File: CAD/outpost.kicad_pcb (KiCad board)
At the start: 2 copper layers, 10 parts, among them U1 SHT41-AD1F-R2, U1 SHT4x, U2 AS7343xDLG, U3 NBM5100B

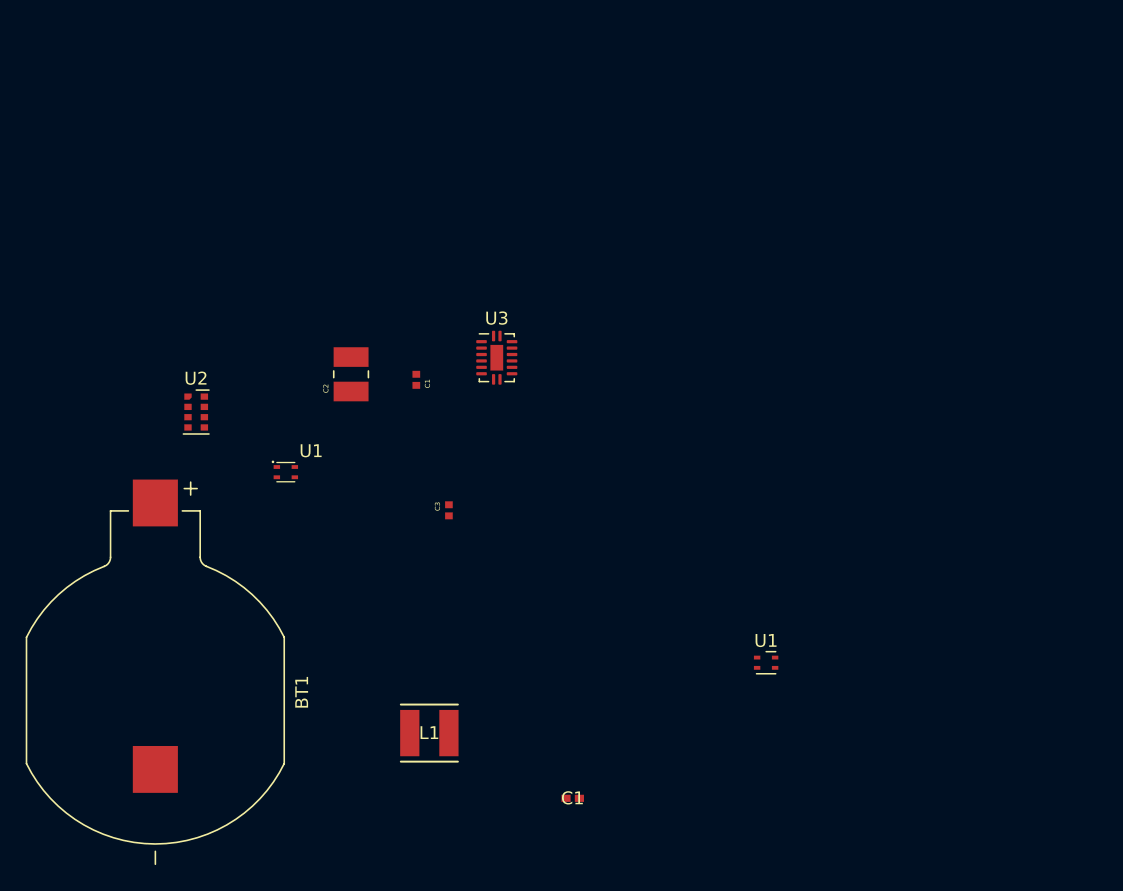
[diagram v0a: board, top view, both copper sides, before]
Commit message: updated libraries
switched to kicad default resistors and capacitors
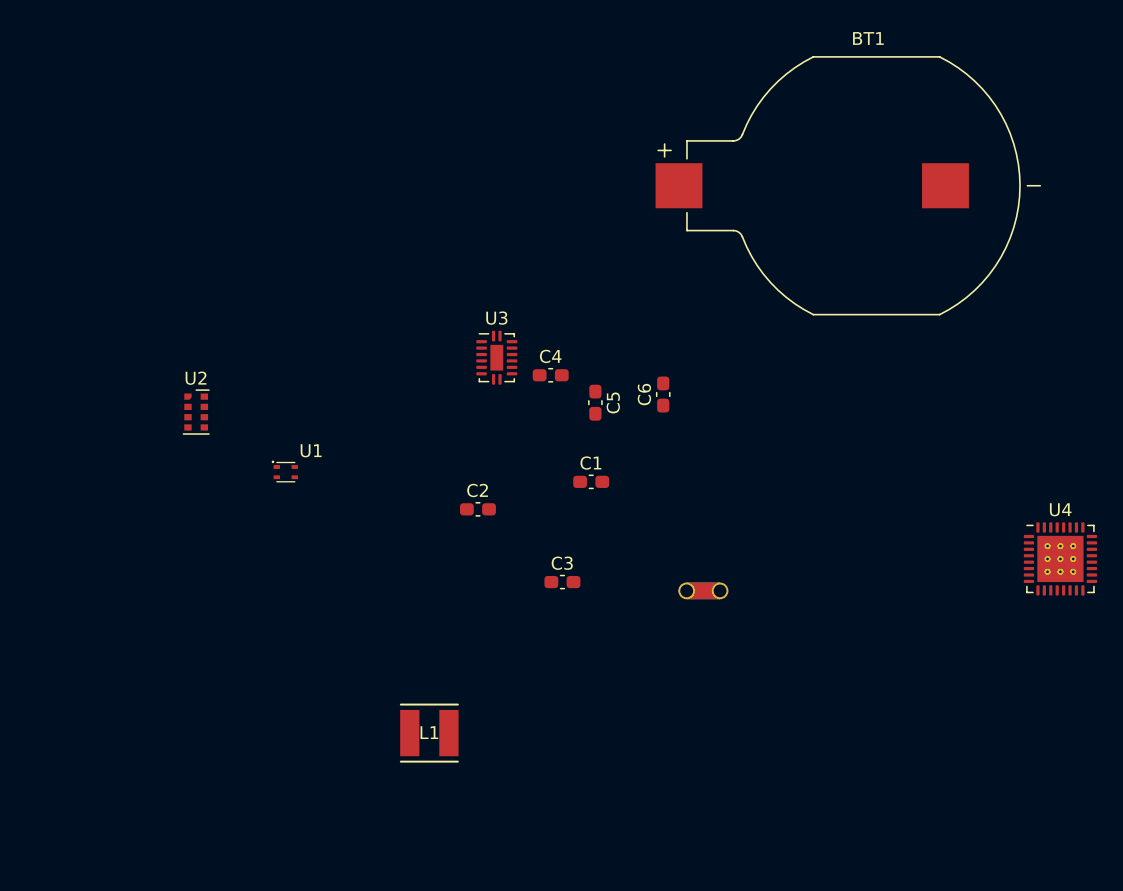
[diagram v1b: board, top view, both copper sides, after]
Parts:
- removed the C1 at (86.4, 41.1)
- removed the C1 at (98.5, 73.7)
- removed the U1 at (113.6, 63.1)
- added C1: 1 uF, Capacitor_SMD:C_0603_1608Metric_Pad1.08x0.95mm_HandSolder, F.Cu at (100.0, 49.0)
- added C4: C, Capacitor_SMD:C_0603_1608Metric_Pad1.08x0.95mm_HandSolder, F.Cu at (96.8, 40.7)
- added C5: C, Capacitor_SMD:C_0603_1608Metric_Pad1.08x0.95mm_HandSolder, F.Cu at (100.3, 42.9)
- added C6: 10 uF, Capacitor_SMD:C_0603_1608Metric_Pad1.08x0.95mm_HandSolder, F.Cu at (105.6, 42.2)
- added NT1: NetTie_2, NetTie:NetTie-2_THT_Pad1.0mm, F.Cu at (107.4, 57.5)
- added U4: nRF52811-QCxx, Package_DFN_QFN:QFN-32-1EP_5x5mm_P0.5mm_EP3.6x3.6mm_ThermalVias, F.Cu at (136.5, 55.0)
- C2: value GRM32EC81C476KE15K -> 47 uF; footprint GRM32EC81C476KE15K:CAPC3225X270N -> Capacitor_SMD:C_0603_1608Metric_Pad1.08x0.95mm_HandSolder
- C3: value GRM155R70J105KA12J -> 1 uF; footprint GRM155R70J105KA12J:CAPC1005X55N -> Capacitor_SMD:C_0603_1608Metric_Pad1.08x0.95mm_HandSolder
- moved BT1 69.0 mm to (122.2, 26.0), turned to 0 degrees
- moved C2 14.4 mm to (91.2, 51.2), turned to 0 degrees
- moved C3 10.5 mm to (97.7, 56.8), turned to 0 degrees
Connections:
- net +3V3 renamed Net-(U3-VDP)
- C2 pad 1: GNDPWR -> +3.3V
- C2 pad 2: +3.3V -> GNDPWR
- U3 pad 10: unconnected-(U3-CAP-Pad10) -> Net-(U3-CAP)
- U3 pad 8: unconnected-(U3-BAL-Pad8) -> Net-(U3-BAL)
